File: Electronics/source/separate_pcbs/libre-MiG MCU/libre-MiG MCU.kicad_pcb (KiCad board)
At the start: 2 copper layers, 130 x 55 mm, 54 parts, among them J1 Conn_01x05, J16 Conn_01x02, J2 Conn_01x03, J3 Conn_01x03, J4 Conn_01x05, J6 Conn_01x20, J7 Conn_01x20, SW10 SW_Push, SW11 SW_Push, SW12 SW_Push, SW13 SW_Push, SW14 SW_Coded, SW4 SW_Push, SW5 SW_SPDT, SW6 SW_SPDT, SW7 SW_SPDT, SW8 SW_Push, SW9 SW_Push, U1 STM32F030C8Tx, U4 FT231XS, U5 ADP122AUJZ-3.3-R7, Y1 ABL-32.000MHZ-B2

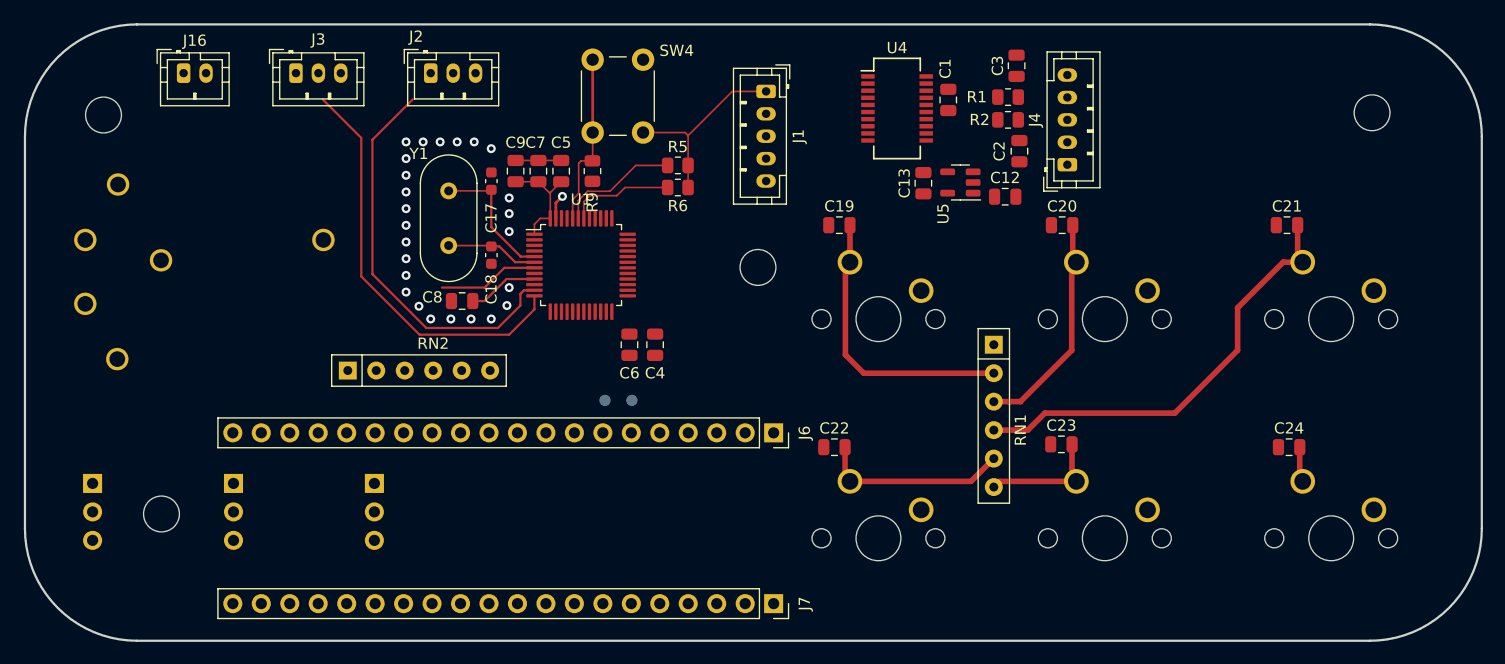
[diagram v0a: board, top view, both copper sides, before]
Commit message: added mechanical ignore
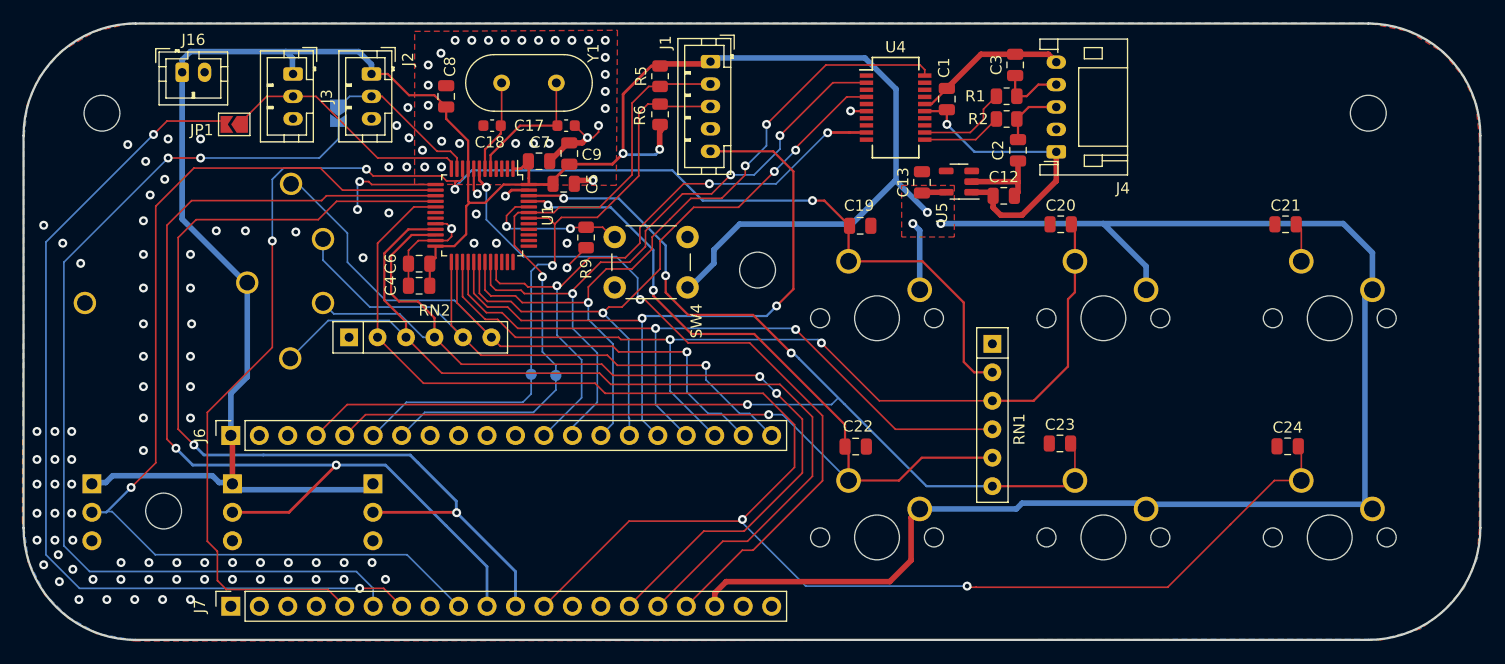
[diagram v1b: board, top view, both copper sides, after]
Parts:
- removed the REF** at (172.0, 156.8)
- removed the REF** at (118.8, 178.8)
- removed the REF** at (226.8, 143.0)
- removed the REF** at (113.6, 143.2)
- added JP1: Jumper_2_Open, Jumper:SolderJumper-2_P1.3mm_Open_TrianglePad1.0x1.5mm, F.Cu at (125.3, 144.0)
- added JP2: Jumper_2_Open, Jumper:SolderJumper-2_P1.3mm_Open_TrianglePad1.0x1.5mm, B.Cu at (134.6, 143.0)
- added REF**: MountingHole_3.2mm_M3, MountingHole:MountingHole_3.2mm_M3, F.Cu at (172.0, 157.0)
- added REF**: MountingHole_3.2mm_M3, MountingHole:MountingHole_3.2mm_M3, F.Cu at (113.5, 143.0)
- added REF**: MountingHole_3.2mm_M3, MountingHole:MountingHole_3.2mm_M3, F.Cu at (226.5, 143.0)
- added REF**: MountingHole_3.2mm_M3, MountingHole:MountingHole_3.2mm_M3, F.Cu at (119.0, 178.5)
- J4: footprint Connector_JST:JST_PH_B5B-PH-K_1x05_P2.00mm_Vertical -> Connector_JST:JST_PH_S5B-PH-K_1x05_P2.00mm_Horizontal
- moved J6 48.4 mm to (125.0, 171.8), turned to 90 degrees
- moved J7 48.4 mm to (125.0, 187.0), turned to 90 degrees
- moved SW7 25.0 mm to (137.7, 176.1)
- moved C4 21.7 mm to (141.8, 158.4), turned to 180 degrees
- moved SW4 20.7 mm to (165.8, 158.6), turned to 180 degrees
- moved C6 20.1 mm to (141.8, 156.4), turned to 180 degrees
- moved C8 18.3 mm to (144.2, 141.5), turned to 90 degrees
- moved Y1 15.3 mm to (149.2, 140.3), turned to 0 degrees
- moved SW6 12.7 mm to (125.1, 176.1)
- moved SW5 12.6 mm to (112.6, 176.1)
- moved C18 11.6 mm to (148.3, 144.1), turned to 0 degrees
- moved U1 9.88 mm to (147.4, 152.1), turned to -90 degrees
- moved C17 8.31 mm to (154.9, 144.1), turned to 180 degrees
- moved R5 8.12 mm to (163.3, 139.7), turned to 90 degrees
- moved TP1 7.14 mm to (154.0, 166.4)
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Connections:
- J6 pad 3: +5V -> (no net)
- J7 pad 6: /MCU/PitchIn -> (no net)
- J7 pad 7: /MCU/YawIn -> (no net)
- J7 pad 8: /MCU/ADC3 -> (no net)
- TP1 pad 1: /IO Controller/SCL -> /MCU/SDA
- TP2 pad 1: /IO Controller/SDA -> /MCU/SCL
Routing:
- net +3V3: track 33.4 -> 352.9 mm, vias 0 -> 5
- net (no net): track 0.00 -> 169.0 mm, vias 0 -> 4
- net /MCU/SW6: track 3.16 -> 146.3 mm, vias 0 -> 2
- net /MCU/SW1: track 25.7 -> 131.9 mm, vias 0 -> 4
- net /MCU/SW5: track 11.0 -> 113.6 mm, vias 0 -> 4
- net /MCU/Togg1: track 0.00 -> 92.5 mm, vias 0 -> 1
- net /MCU/Togg2: track 0.00 -> 92.0 mm, vias 0 -> 2
- net /MCU/Rot1: track 0.00 -> 89.2 mm
- net /MCU/SW4: track 16.9 -> 105.8 mm, vias 0 -> 3
- net /MCU/Togg3: track 0.00 -> 87.9 mm, vias 0 -> 2
- net /MCU/Rot2: track 0.00 -> 86.9 mm, vias 0 -> 2
- net /MCU/RxD: track 0.00 -> 67.9 mm, vias 0 -> 3
- net /MCU/SW2: track 20.3 -> 85.5 mm, vias 0 -> 2
- net /MCU/EN: track 0.00 -> 63.2 mm, vias 0 -> 2
- net /MCU/Rot4: track 0.00 -> 61.3 mm, vias 0 -> 1
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- added copper zone on F.Cu, net +3V3
- added copper zone on B.Cu, net GND
- added copper zone on F.Cu, net GND
